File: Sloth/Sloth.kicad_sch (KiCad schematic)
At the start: 20 parts, among them J1 AudioJack2_SwitchT, J2 AudioJack2_SwitchT, U1 TL074

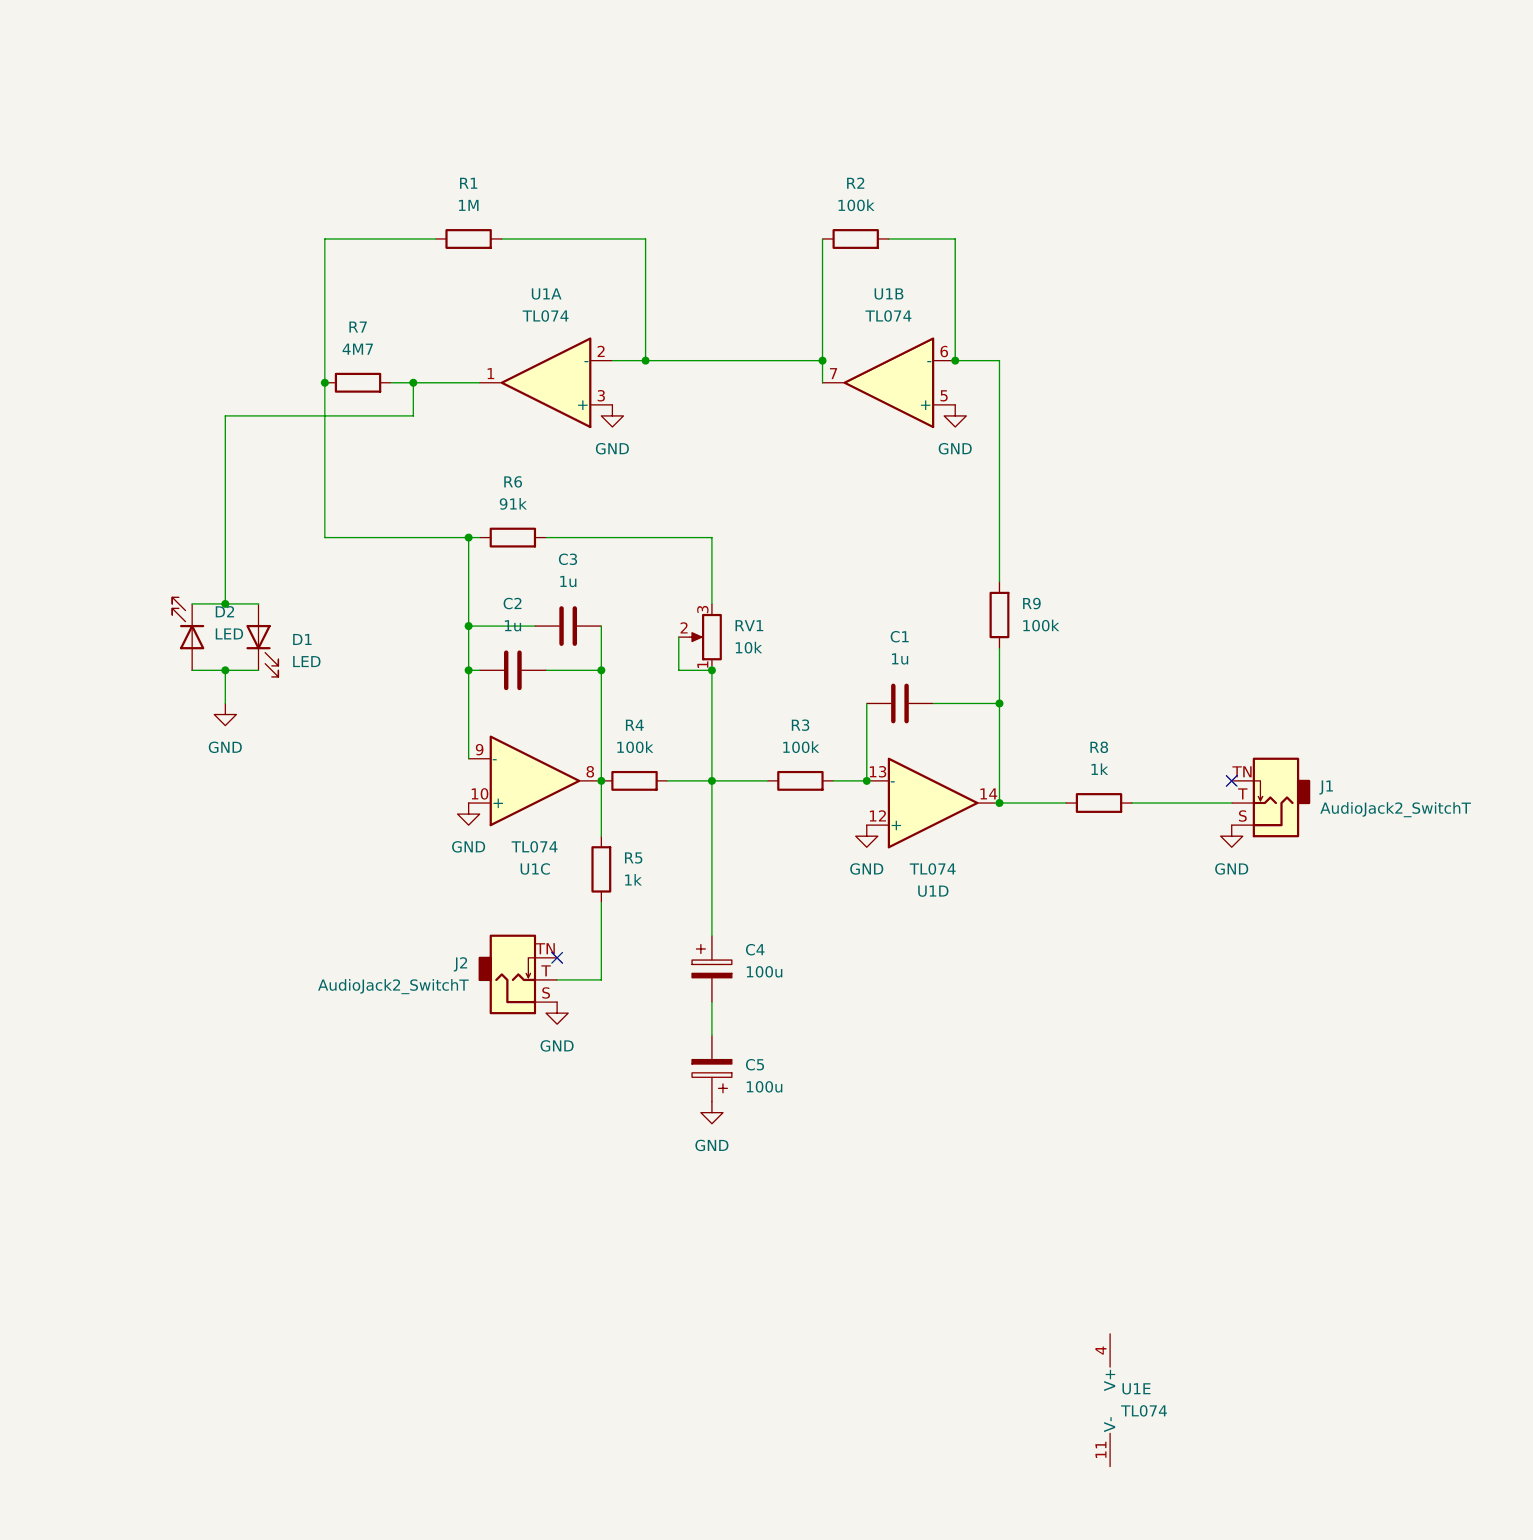
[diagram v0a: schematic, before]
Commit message: work on slot
schematic, pcb done. Panel started
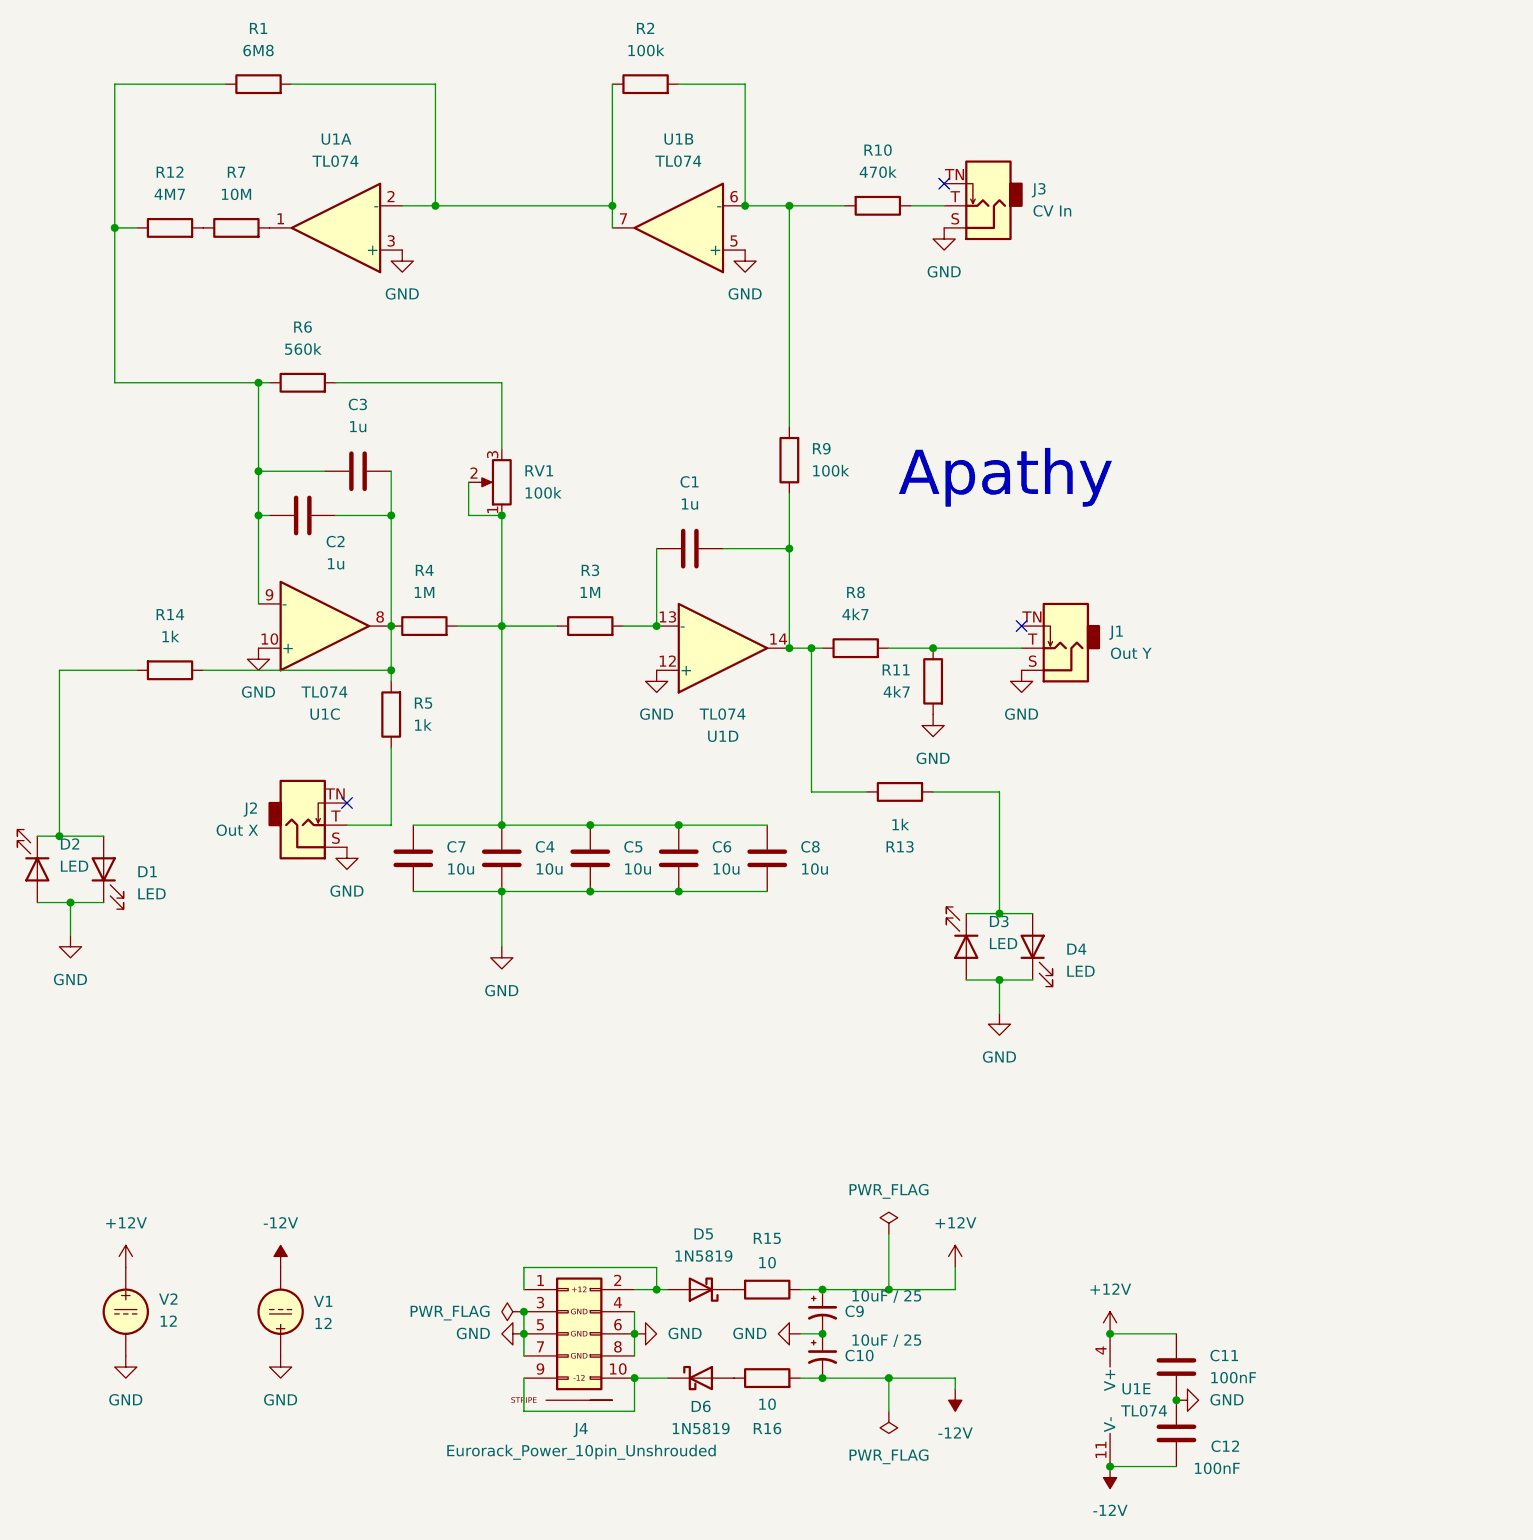
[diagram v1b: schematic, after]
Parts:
- removed C4, C5: 100u, symbol Device:C_Polarized
- added C10, C9: 10uF / 25, Capacitor_THT:CP_Radial_D4.0mm_P2.00mm, symbol PCM_4ms_Capacitor:47uF_5x5.3_16V
- added C11, C12: 100nF, Capacitor_SMD:C_0805_2012Metric_Pad1.18x1.45mm_HandSolder, symbol Device:C
- added C4, C5, C6, C7, C8: 10u, Capacitor_SMD:C_0805_2012Metric_Pad1.18x1.45mm_HandSolder, symbol Device:C
- added D3, D4: LED, LED_THT:LED_D3.0mm, symbol Device:LED
- added D5, D6: 1N5819, Diode_THT:D_DO-41_SOD81_P2.54mm_Vertical_AnodeUp, symbol Diode:1N5819
- added J3: CV In, mort_mix:PJ398SM, symbol Connector_Audio:AudioJack2_SwitchT
- added J4: Eurorack_Power_10pin_Unshrouded, mort_mix:PinHeader_2x05_P2.54mm_Vertical_shrouded, symbol PCM_4ms_Connector:Eurorack_Power_10pin_Unshrouded
- added R10: 470k, Resistor_SMD:R_0805_2012Metric_Pad1.20x1.40mm_HandSolder, symbol Device:R
- added R11: 4k7, Resistor_SMD:R_0805_2012Metric_Pad1.20x1.40mm_HandSolder, symbol Device:R
- added R12: 4M7, Resistor_SMD:R_0805_2012Metric_Pad1.20x1.40mm_HandSolder, symbol Device:R
- added R13, R14: 1k, Resistor_SMD:R_0805_2012Metric_Pad1.20x1.40mm_HandSolder, symbol Device:R
- added R15, R16: 10, Resistor_THT:R_Axial_DIN0204_L3.6mm_D1.6mm_P1.90mm_Vertical, symbol Device:R
- added V1, V2: 12, symbol Simulation_SPICE:VDC
- C1, C2, C3: footprint (none) -> Capacitor_SMD:C_0805_2012Metric_Pad1.18x1.45mm_HandSolder
- D1, D2: footprint (none) -> LED_THT:LED_D3.0mm
- J1: value AudioJack2_SwitchT -> Out Y; footprint (none) -> mort_mix:PJ398SM
- J2: value AudioJack2_SwitchT -> Out X; footprint (none) -> mort_mix:PJ398SM
- R1: value 1M -> 6M8; footprint (none) -> Resistor_SMD:R_0805_2012Metric_Pad1.20x1.40mm_HandSolder
- R2, R5, R9: footprint (none) -> Resistor_SMD:R_0805_2012Metric_Pad1.20x1.40mm_HandSolder
- R3, R4: value 100k -> 1M; footprint (none) -> Resistor_SMD:R_0805_2012Metric_Pad1.20x1.40mm_HandSolder
- R6: value 91k -> 560k; footprint (none) -> Resistor_SMD:R_0805_2012Metric_Pad1.20x1.40mm_HandSolder
- R7: value 4M7 -> 10M; footprint (none) -> Resistor_SMD:R_0805_2012Metric_Pad1.20x1.40mm_HandSolder
- R8: value 1k -> 4k7; footprint (none) -> Resistor_SMD:R_0805_2012Metric_Pad1.20x1.40mm_HandSolder
- RV1: value 10k -> 100k; footprint (none) -> mort_mix:Potentiometer_Alpha_RD901F-40-00D_Single_Vertical_withhole
- U1: footprint (none) -> Package_SO:SO-14_3.9x8.65mm_P1.27mm
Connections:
- net GND: now also C10.1, C11.1, C12.2, C4.1, C5.1, C6.1, C7.1, C8.1, C9.2, D3.2 (A), D4.1 (K), J3.S, J4.3 (GND), J4.4 (GND), J4.5 (GND), J4.6 (GND), J4.7 (GND), J4.8 (GND), R11.2, V1.1, V2.2
- net at C2.1, C3.1, R1.1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: now also R12.1; no longer R7.1
- net at R7.2, U1.1: no longer D1.2 (A), D2.1 (K)
- net at J1.T, R8.2: now also R11.1
- net at C2.2, C3.2, R4.1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: now also R14.1
- net -12V: now reaches U1.11 (V-)
- net -12V: now also C10.2, C12.1, R16.2, V1.2
- net +12V: now reaches U1.4 (V+)
- net +12V: now also C11.2, C9.1, R15.1, V2.1
- net at C1.2, R8.1, R9.1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: now also R13.1
- net at R2.2, R9.2, U1.6 (-): now also R10.2
- net at R3.1, R4.2, RV1.1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: now also C4.2, C5.2, C6.2, C7.2, C8.2
- new net: R12.2, R7.1
- new net: J3.T, R10.1
- new net: D1.2 (A), D2.1 (K), R14.2
- new net: D5.2 (A), J4.1 (+12V), J4.2 (+12V)
- new net: D6.1 (K), J4.10 (-12V), J4.9 (-12V)
- new net: D3.1 (K), D4.2 (A), R13.2
- new net: D6.2 (A), R16.1
- new net: D5.1 (K), R15.2
- no-connect marks 2 -> 3
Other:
- note added: "Apathy"
- moved on the sheet: C1, C2, C3, D1, D2, J1, J2, R1, R2, R3, R4, R5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
